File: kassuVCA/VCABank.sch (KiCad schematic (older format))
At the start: 11 parts, among them U301 TL074

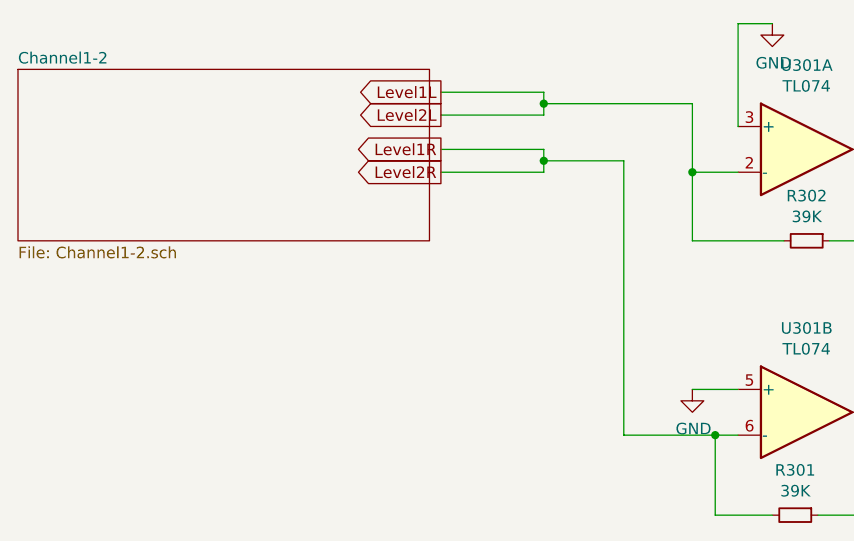
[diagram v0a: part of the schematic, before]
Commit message: WIP 0805 TL072 dual channel
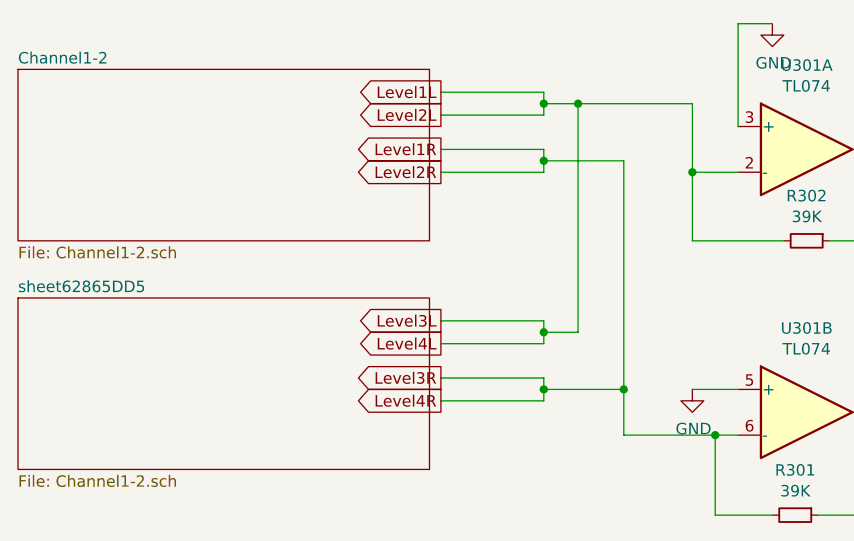
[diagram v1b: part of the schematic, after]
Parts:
- R301, R302, R303, R304, R305, R306, R307, R308: footprint Resistor_THT:R_Axial_DIN0207_L6.3mm_D2.5mm_P7.62mm_Horizontal -> Resistor_SMD:R_0805_2012Metric_Pad1.20x1.40mm_HandSolder
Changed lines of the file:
@@
 $Descr A4 11693 8268
 encoding utf-8
-Sheet 3 4
+Sheet 3 5
 Title ""
 Date ""
@@
 F 0 "R302" V 4004 1550 50  0000 C CNN
 F 1 "39K" V 4095 1550 50  0000 C CNN
-F 2 "Resistor_THT:R_Axial_DIN0207_L6.3mm_D2.5mm_P7.62mm_Horizontal" H 4200 1550 50  0001 C CNN
+F 2 "Resistor_SMD:R_0805_2012Metric_Pad1.20x1.40mm_HandSolder" H 4200 1550 50  0001 C CNN
 F 3 "~" H 4200 1550 50  0001 C CNN
 	1    4200 1550
@@
 F 0 "R303" V 4604 1550 50  0000 C CNN
 F 1 "2K" V 4695 1550 50  0000 C CNN
-F 2 "Resistor_THT:R_Axial_DIN0207_L6.3mm_D2.5mm_P7.62mm_Horizontal" H 4800 1550 50  0001 C CNN
+F 2 "Resistor_SMD:R_0805_2012Metric_Pad1.20x1.40mm_HandSolder" H 4800 1550 50  0001 C CNN
 F 3 "~" H 4800 1550 50  0001 C CNN
 	1    4800 1550
@@
 F 0 "R305" V 5704 1900 50  0000 C CNN
 F 1 "100K" V 5795 1900 50  0000 C CNN
-F 2 "Resistor_THT:R_Axial_DIN0207_L6.3mm_D2.5mm_P7.62mm_Horizontal" H 5900 1900 50  0001 C CNN
+F 2 "Resistor_SMD:R_0805_2012Metric_Pad1.20x1.40mm_HandSolder" H 5900 1900 50  0001 C CNN
 F 3 "~" H 5900 1900 50  0001 C CNN
 	1    5900 1900
@@
 F 0 "R308" V 6304 1150 50  0000 C CNN
 F 1 "1K" V 6395 1150 50  0000 C CNN
-F 2 "Resistor_THT:R_Axial_DIN0207_L6.3mm_D2.5mm_P7.62mm_Horizontal" H 6500 1150 50  0001 C CNN
+F 2 "Resistor_SMD:R_0805_2012Metric_Pad1.20x1.40mm_HandSolder" H 6500 1150 50  0001 C CNN
 F 3 "~" H 6500 1150 50  0001 C CNN
 	1    6500 1150
@@
 F 0 "R301" V 3954 2750 50  0000 C CNN
 F 1 "39K" V 4045 2750 50  0000 C CNN
-F 2 "Resistor_THT:R_Axial_DIN0207_L6.3mm_D2.5mm_P7.62mm_Horizontal" H 4150 2750 50  0001 C CNN
+F 2 "Resistor_SMD:R_0805_2012Metric_Pad1.20x1.40mm_HandSolder" H 4150 2750 50  0001 C CNN
 F 3 "~" H 4150 2750 50  0001 C CNN
 	1    4150 2750
@@
 F 0 "R304" V 4604 2300 50  0000 C CNN
 F 1 "2K" V 4695 2300 50  0000 C CNN
-F 2 "Resistor_THT:R_Axial_DIN0207_L6.3mm_D2.5mm_P7.62mm_Horizontal" H 4800 2300 50  0001 C CNN
+F 2 "Resistor_SMD:R_0805_2012Metric_Pad1.20x1.40mm_HandSolder" H 4800 2300 50  0001 C CNN
 F 3 "~" H 4800 2300 50  0001 C CNN
 	1    4800 2300
@@
 F 0 "R306" V 5704 2750 50  0000 C CNN
 F 1 "100K" V 5795 2750 50  0000 C CNN
-F 2 "Resistor_THT:R_Axial_DIN0207_L6.3mm_D2.5mm_P7.62mm_Horizontal" H 5900 2750 50  0001 C CNN
+F 2 "Resistor_SMD:R_0805_2012Metric_Pad1.20x1.40mm_HandSolder" H 5900 2750 50  0001 C CNN
 F 3 "~" H 5900 2750 50  0001 C CNN
 	1    5900 2750
@@
 F 0 "R307" V 6254 2300 50  0000 C CNN
 F 1 "1K" V 6345 2300 50  0000 C CNN
-F 2 "Resistor_THT:R_Axial_DIN0207_L6.3mm_D2.5mm_P7.62mm_Horizontal" H 6450 2300 50  0001 C CNN
+F 2 "Resistor_SMD:R_0805_2012Metric_Pad1.20x1.40mm_HandSolder" H 6450 2300 50  0001 C CNN
 F 3 "~" H 6450 2300 50  0001 C CNN
 	1    6450 2300
@@
 	6600 1150 7100 1150
 Wire Wire Line
-	3050 950  3700 950
-Wire Wire Line
-	3400 1200 3400 2400
+	3050 950  3200 950
+Wire Wire Line
+	3400 1200 3400 2200
 Wire Wire Line
 	5900 1450 5900 1550
+Text GLabel 2600 1900 0    50   Output ~ 0
+Level3L
+Text GLabel 2600 2000 0    50   Output ~ 0
+Level4L
+Text GLabel 2600 2150 0    50   Output ~ 0
+Level3R
+Text GLabel 2600 2250 0    50   Output ~ 0
+Level4R
+Wire Wire Line
+	2600 1900 3050 1900
+Wire Wire Line
+	3050 2000 2600 2000
+Wire Wire Line
+	2600 2150 3050 2150
+Wire Wire Line
+	3050 2250 2600 2250
+$Sheet
+S 750  1800 1800 750
+U 62865DD7
+F0 "sheet62865DD5" 50
+F1 "Channel1-2.sch" 50
+$EndSheet
+Wire Wire Line
+	3050 2150 3050 2200
+Wire Wire Line
+	3050 2000 3050 1950
+Wire Wire Line
+	3050 1950 3200 1950
+Wire Wire Line
+	3200 1950 3200 950
+Connection ~ 3050 1950
+Wire Wire Line
+	3050 1950 3050 1900
+Connection ~ 3200 950
+Wire Wire Line
+	3200 950  3700 950
+Wire Wire Line
+	3050 2200 3400 2200
+Connection ~ 3050 2200
+Wire Wire Line
+	3050 2200 3050 2250
+Connection ~ 3400 2200
+Wire Wire Line
+	3400 2200 3400 2400
 $EndSCHEMATC

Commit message: 4/6 channels, 4 routed
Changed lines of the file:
@@
 $Descr A4 11693 8268
 encoding utf-8
-Sheet 3 5
+Sheet 3 6
 Title ""
 Date ""
@@
 S 750  1800 1800 750
 U 62865DD7
-F0 "sheet62865DD5" 50
+F0 "Channel3-4" 50
 F1 "Channel1-2.sch" 50
 $EndSheet
@@
 Wire Wire Line
 	3400 2200 3400 2400
+Text GLabel 2600 2950 0    50   Output ~ 0
+Level5L
+Text GLabel 2600 3050 0    50   Output ~ 0
+Level6L
+Text GLabel 2600 3200 0    50   Output ~ 0
+Level5R
+Text GLabel 2600 3300 0    50   Output ~ 0
+Level6R
+Wire Wire Line
+	2600 2950 3050 2950
+Wire Wire Line
+	3050 3050 2600 3050
+Wire Wire Line
+	2600 3200 3050 3200
+Wire Wire Line
+	3050 3300 2600 3300
+$Sheet
+S 750  2850 1800 750
+U 625C0132
+F0 "Channel5-6" 50
+F1 "Channel5-6.sch" 50
+$EndSheet
+Wire Wire Line
+	3050 3200 3050 3250
+Wire Wire Line
+	3050 2950 3050 3000
+Wire Wire Line
+	3050 3250 3400 3250
+Wire Wire Line
+	3400 3250 3400 2400
+Connection ~ 3050 3250
+Wire Wire Line
+	3050 3250 3050 3300
+Connection ~ 3400 2400
+Wire Wire Line
+	3050 3000 3200 3000
+Wire Wire Line
+	3200 3000 3200 1950
+Connection ~ 3050 3000
+Wire Wire Line
+	3050 3000 3050 3050
+Connection ~ 3200 1950
 $EndSCHEMATC

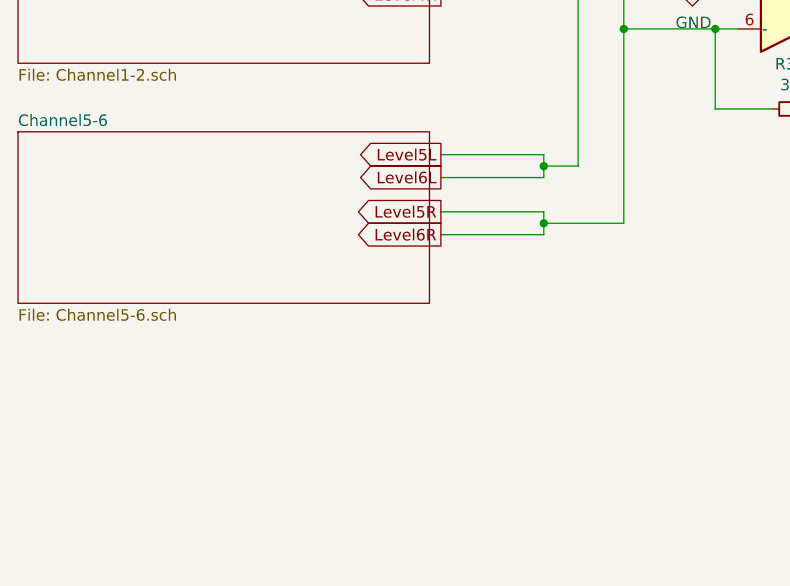
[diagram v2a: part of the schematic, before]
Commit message: mixer WIP, 8 channels, more or less
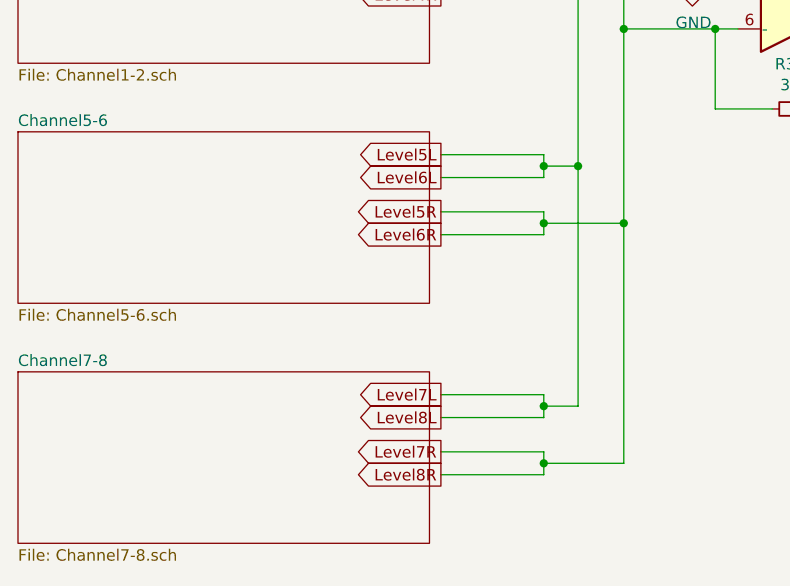
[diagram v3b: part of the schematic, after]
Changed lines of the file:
@@
 $Descr A4 11693 8268
 encoding utf-8
-Sheet 3 6
+Sheet 3 7
 Title ""
 Date ""
@@
 	3050 3000 3050 3050
 Connection ~ 3200 1950
+Text GLabel 2600 4000 0    50   Output ~ 0
+Level7L
+Text GLabel 2600 4100 0    50   Output ~ 0
+Level8L
+Text GLabel 2600 4250 0    50   Output ~ 0
+Level7R
+Text GLabel 2600 4350 0    50   Output ~ 0
+Level8R
+Wire Wire Line
+	2600 4000 3050 4000
+Wire Wire Line
+	3050 4100 2600 4100
+Wire Wire Line
+	2600 4250 3050 4250
+Wire Wire Line
+	3050 4350 2600 4350
+$Sheet
+S 750  3900 1800 750
+U 62792C39
+F0 "Channel7-8" 50
+F1 "Channel7-8.sch" 50
+$EndSheet
+Wire Wire Line
+	3050 4100 3050 4050
+Wire Wire Line
+	3050 4350 3050 4300
+Wire Wire Line
+	3050 4050 3200 4050
+Wire Wire Line
+	3200 4050 3200 3000
+Connection ~ 3050 4050
+Wire Wire Line
+	3050 4050 3050 4000
+Connection ~ 3200 3000
+Wire Wire Line
+	3050 4300 3400 4300
+Wire Wire Line
+	3400 4300 3400 3250
+Connection ~ 3050 4300
+Wire Wire Line
+	3050 4300 3050 4250
+Connection ~ 3400 3250
 $EndSCHEMATC
